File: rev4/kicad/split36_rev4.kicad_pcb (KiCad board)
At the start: 2 copper layers, 121 x 97.4 mm, 115 parts, among them SW1 SW_SPDT, SW2 SW_SPDT, SW3 Switch, SW4 Switch, U1 Nice_Nano_V2

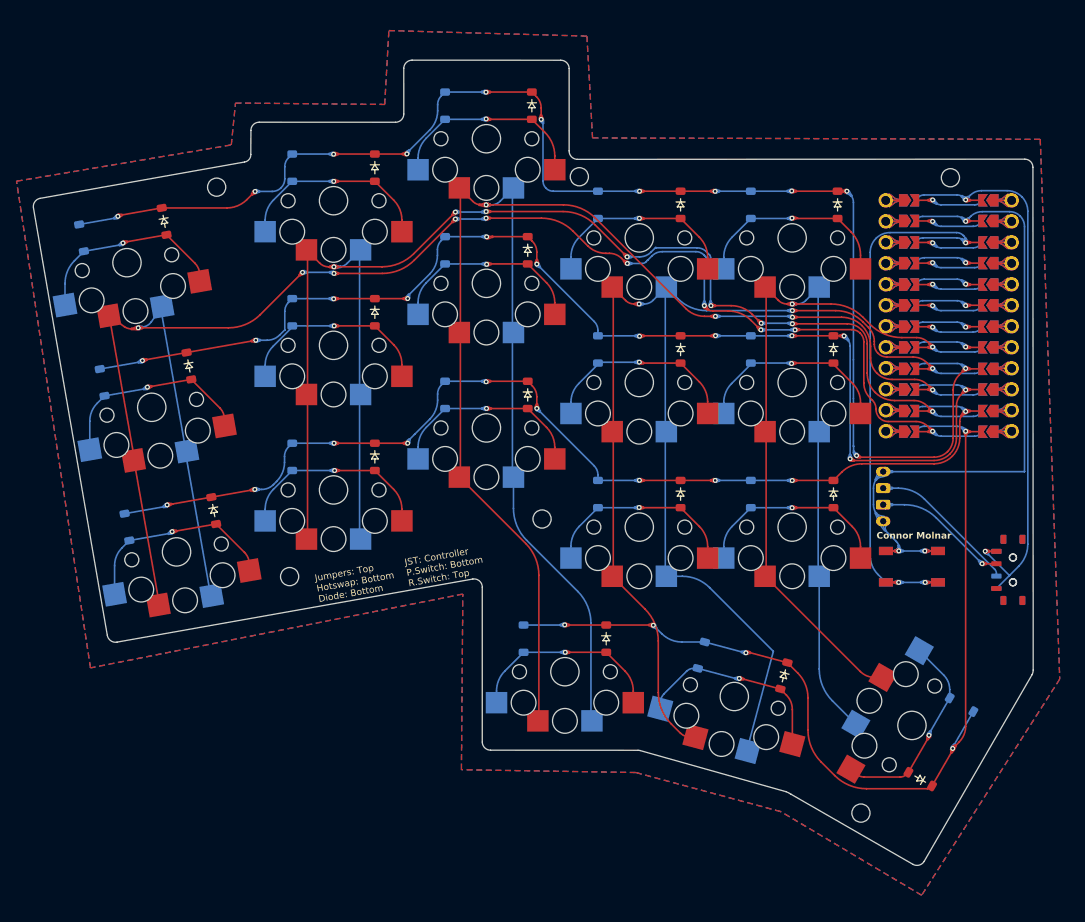
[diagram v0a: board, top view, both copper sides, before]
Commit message: wrapping up 3d prints for rev4
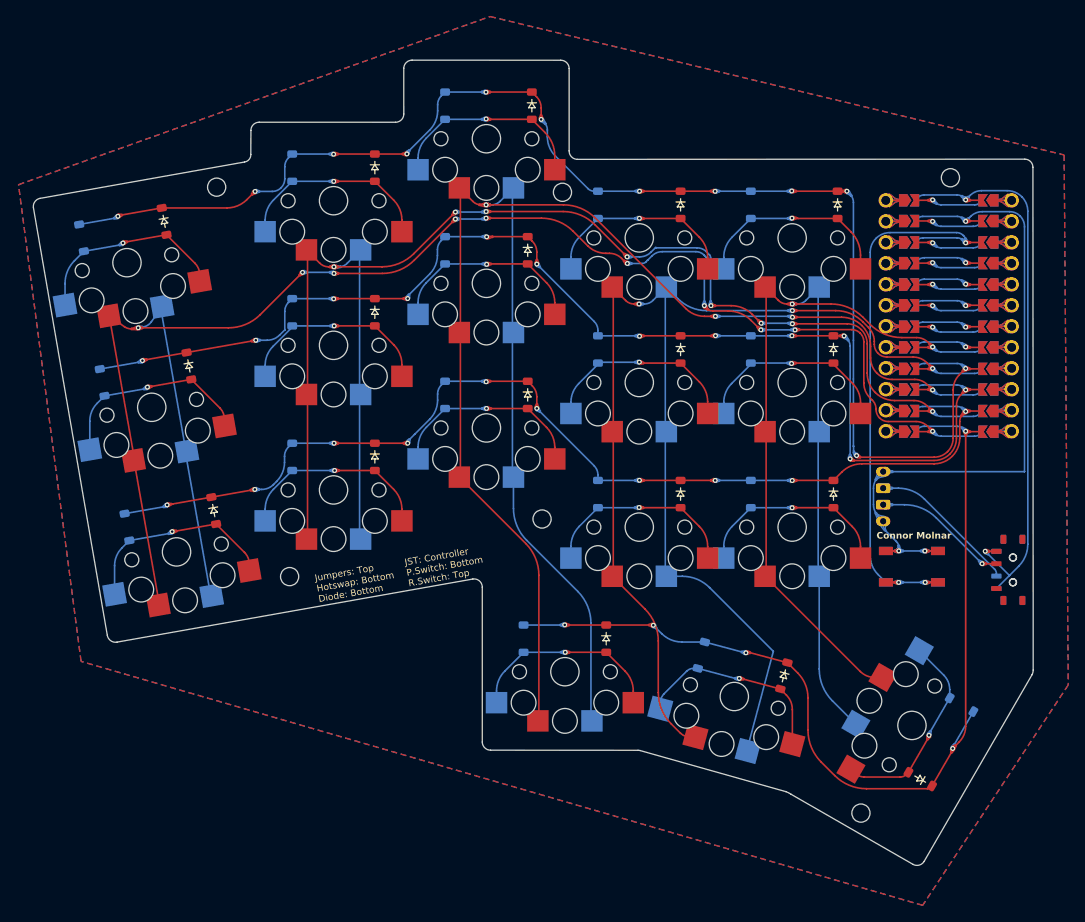
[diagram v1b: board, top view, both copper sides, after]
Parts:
- moved H6 2.77 mm to (143.6, 60.8)
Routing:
- net Via21: track 175.2 -> 172.1 mm
